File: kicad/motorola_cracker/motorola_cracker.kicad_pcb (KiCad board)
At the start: 2 copper layers, 134 x 39.4 mm, 27 parts, among them J1 DB9, P1 CONN_6, P2 CONN_2, P3 CONN_6, U1 78L10, U2 74LS245, U3 MAX232, U4 78L05, U5 68HC05_PLCC, X1 4Mhz

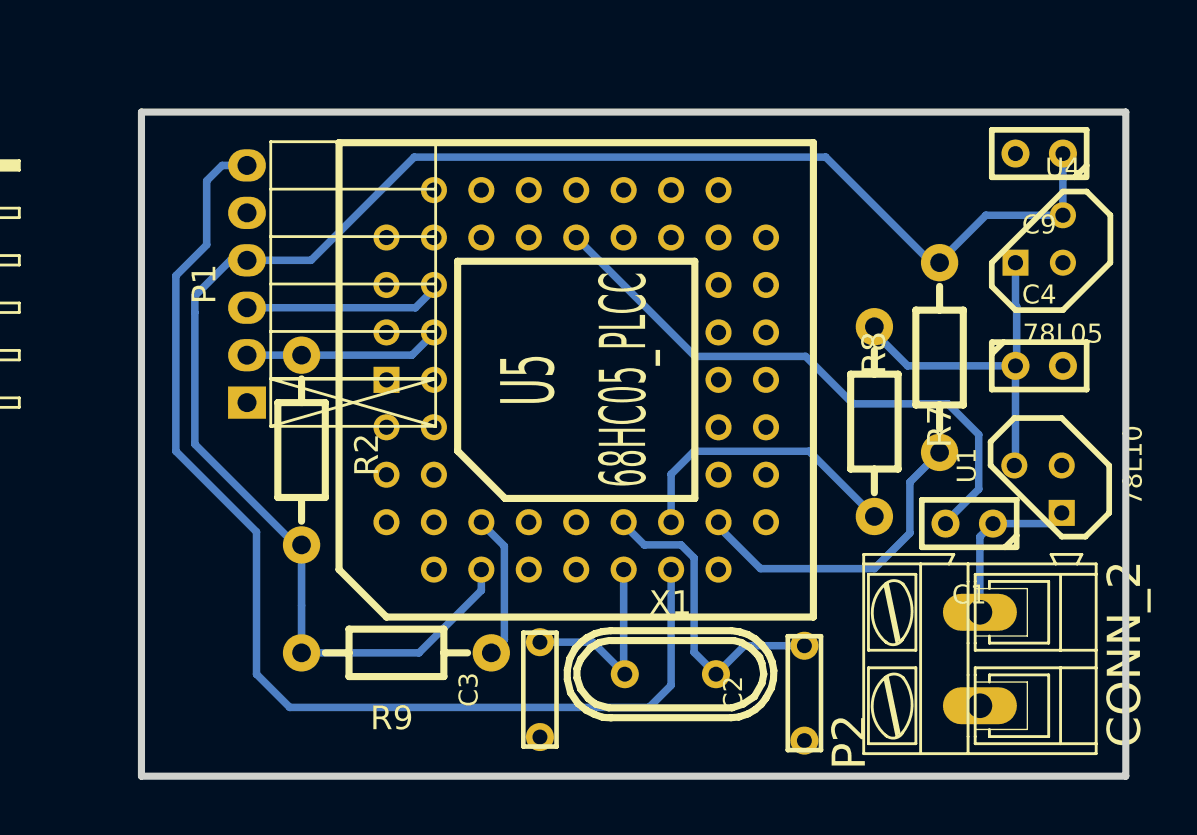
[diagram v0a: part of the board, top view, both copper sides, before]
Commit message: update cpu board to fit 50x50cm for dirtypcb servis req.
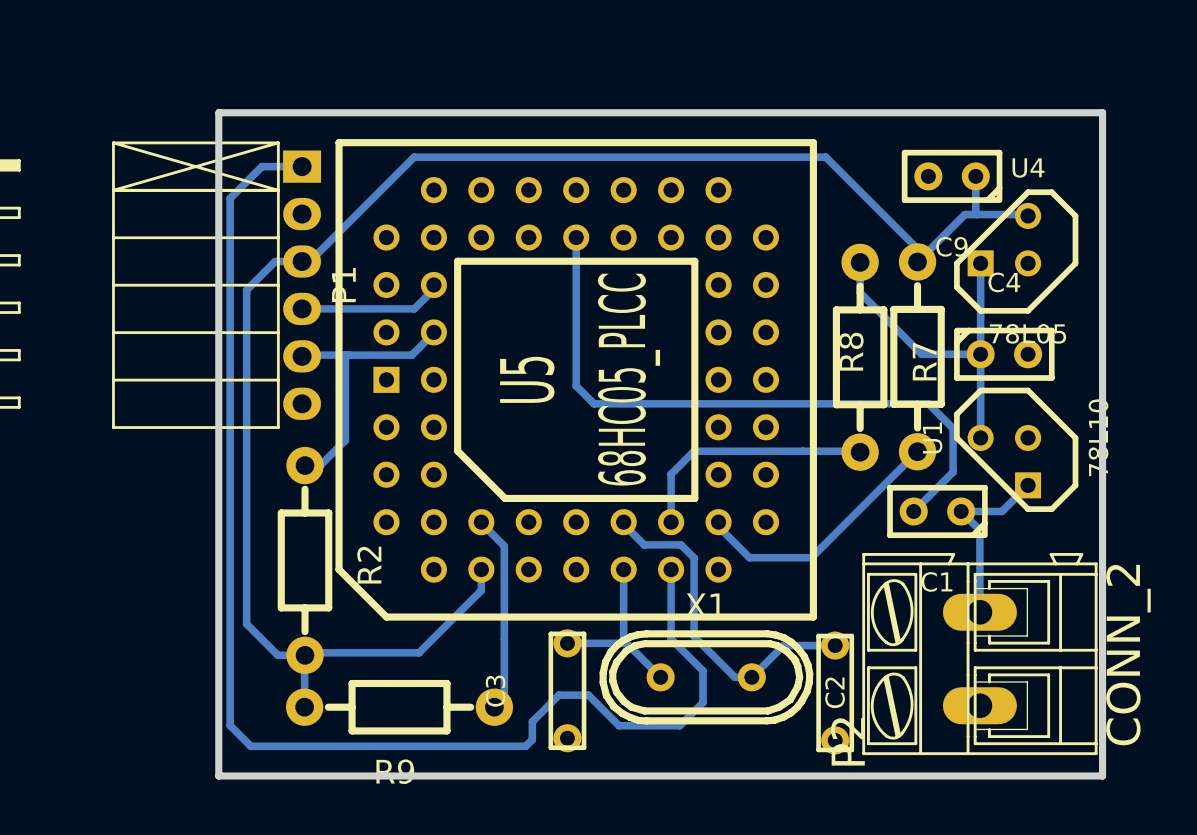
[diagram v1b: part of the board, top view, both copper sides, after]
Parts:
- moved R2 5.91 mm to (189.1, 108.5)
- moved C9 4.82 mm to (223.7, 87.9)
- moved R7 3.53 mm to (218.8, 97.6)
- moved P1 2.95 mm to (188.9, 93.7), turned to 90 degrees
- moved R9 2.92 mm to (194.2, 116.3)
- moved U1 2.33 mm to (226.5, 103.2)
- moved C4 1.97 mm to (226.5, 97.4)
- moved X1 1.93 mm to (210.6, 114.7)
- moved U4 1.87 mm to (226.5, 91.3)
- moved C1 1.82 mm to (223.0, 105.8)
- moved C2 1.65 mm to (217.5, 115.6)
- moved C3 1.47 mm to (203.1, 115.4)
- moved R8 1.18 mm to (221.9, 97.6)
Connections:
- net Tx renamed TX
- P1 pad 1: GND -> 68_18
- P1 pad 2: 68_52 -> (no net)
- P1 pad 3: 68_50 -> +5V
- P1 pad 4: +5V -> 68_50
- P1 pad 5: (no net) -> 68_52
- P1 pad 6: 68_18 -> GND
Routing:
- net 68_18: track 85.2 -> 93.5 mm
- net 68_52: track 22.0 -> 26.7 mm
- net Net-(R8-Pad1): track 17.4 -> 14.1 mm
- net GND: track 32.6 -> 35.8 mm
- net 68_50: track 22.1 -> 19.4 mm
- net +5V: track 114.9 -> 112.5 mm
- net Net-(R7-Pad2): track 15.5 -> 13.3 mm
- net Net-(R9-Pad1): track 9.29 -> 11.1 mm
- net Net-(C2-Pad2): track 17.1 -> 18.4 mm
- net Net-(C3-Pad2): track 10.9 -> 9.73 mm
- net Net-(C1-Pad1): track 8.96 -> 9.97 mm
- net +10V: track 19.5 -> 18.8 mm
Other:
- board size 134 x 39.4 mm -> 132.7 x 39.4 mm

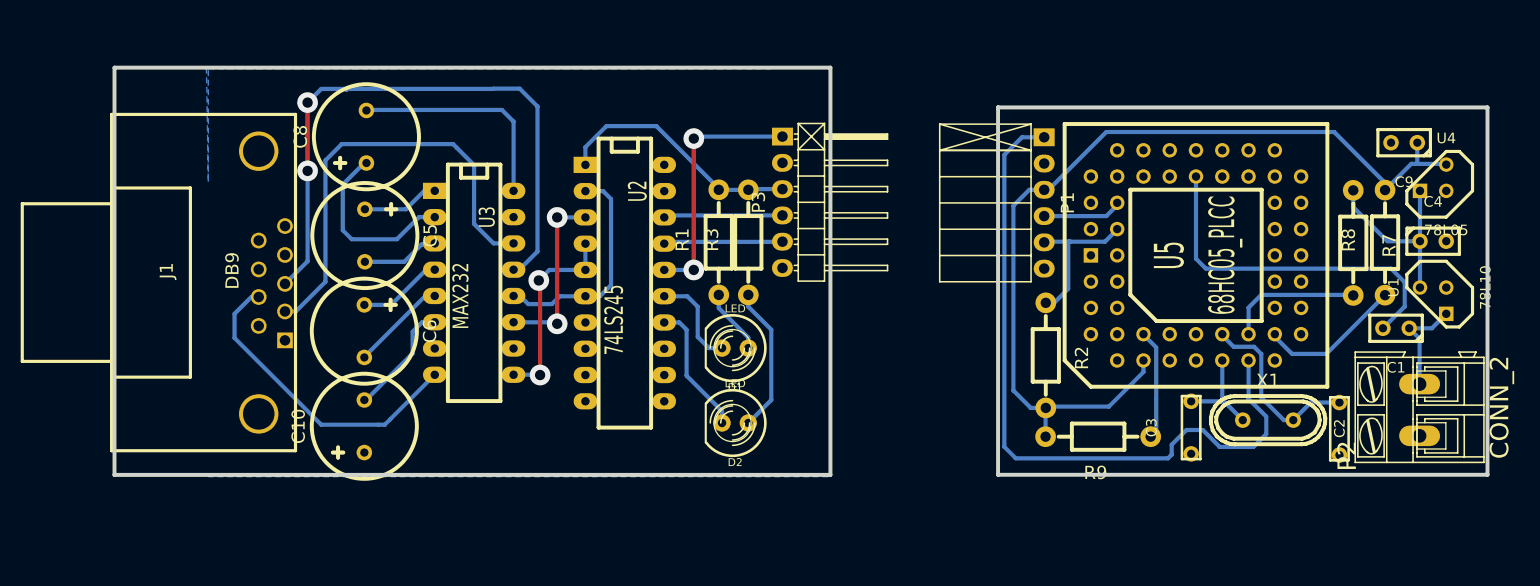
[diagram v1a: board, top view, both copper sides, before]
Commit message: remke pcb's to match 5x5cm
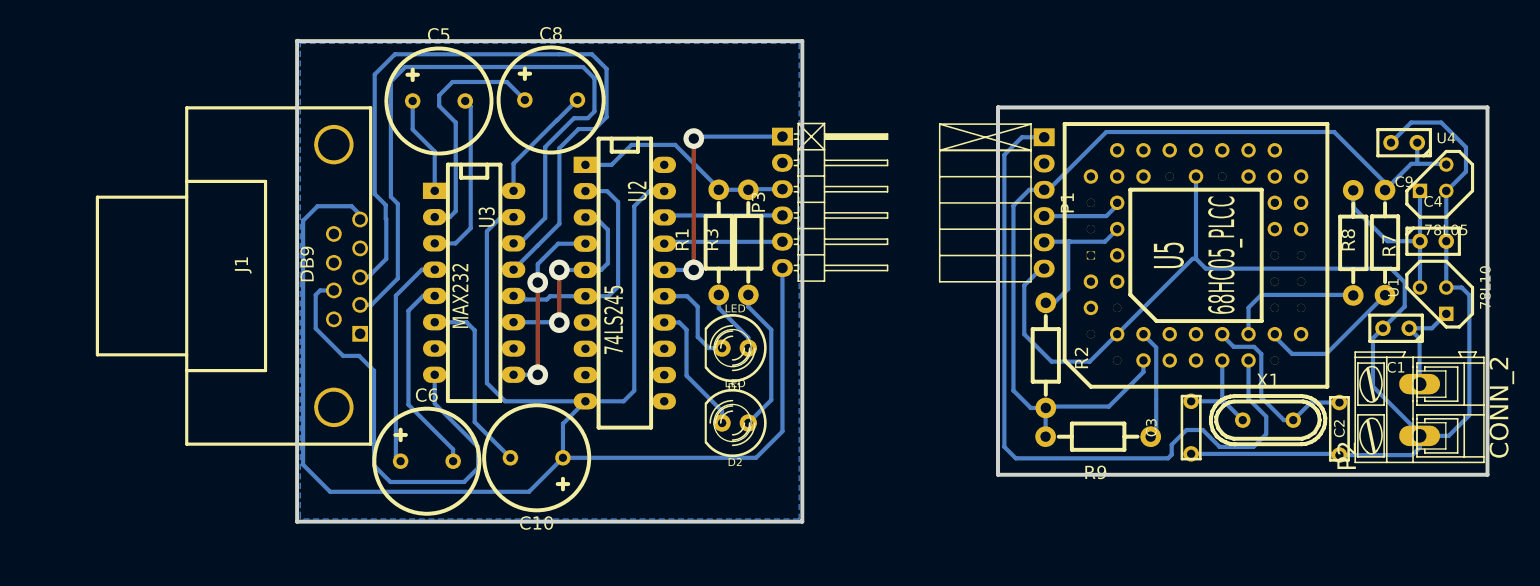
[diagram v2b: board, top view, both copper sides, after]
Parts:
- moved C8 18.2 mm to (141.3, 83.8), turned to 0 degrees
- moved C10 16.9 mm to (139.9, 118.4), turned to 180 degrees
- moved C5 14.8 mm to (130.4, 83.9), turned to 0 degrees
- moved C6 14.0 mm to (129.3, 118.7), turned to 0 degrees
- moved J1 7.29 mm to (121.5, 100.9)
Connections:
- U2 pad 5: Reset -> TX
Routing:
- net GND: track 35.8 -> 300.5 mm
- net Net-(J1-Pad2): track 43.0 -> 65.7 mm
- net Net-(C6-Pad1): track 8.22 -> 21.8 mm
- net Net-(J1-Pad7): track 30.2 -> 43.7 mm
- net Net-(C6-Pad2): track 9.30 -> 20.4 mm
- net Net-(J1-Pad3): track 59.4 -> 69.5 mm, vias 2 -> 0
- net Net-(C8-Pad2): track 21.4 -> 11.4 mm
- net Net-(C5-Pad2): track 7.49 -> 16.7 mm
- net Net-(C10-Pad2): track 11.3 -> 18.1 mm
- net Net-(C8-Pad1): track 17.7 -> 23.7 mm
- net TX: track 17.4 -> 20.5 mm
- net +5V: track 112.5 -> 110.0 mm
- net Net-(C5-Pad1): track 7.49 -> 9.57 mm
- net Reset: track 20.2 -> 18.5 mm
- net Rx: track 21.9 -> 22.8 mm
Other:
- board size 132.7 x 39.4 mm -> 115.1 x 46.5 mm
- net class Default: via_dia 2 -> 2.4; via_drill 1 -> 1.2

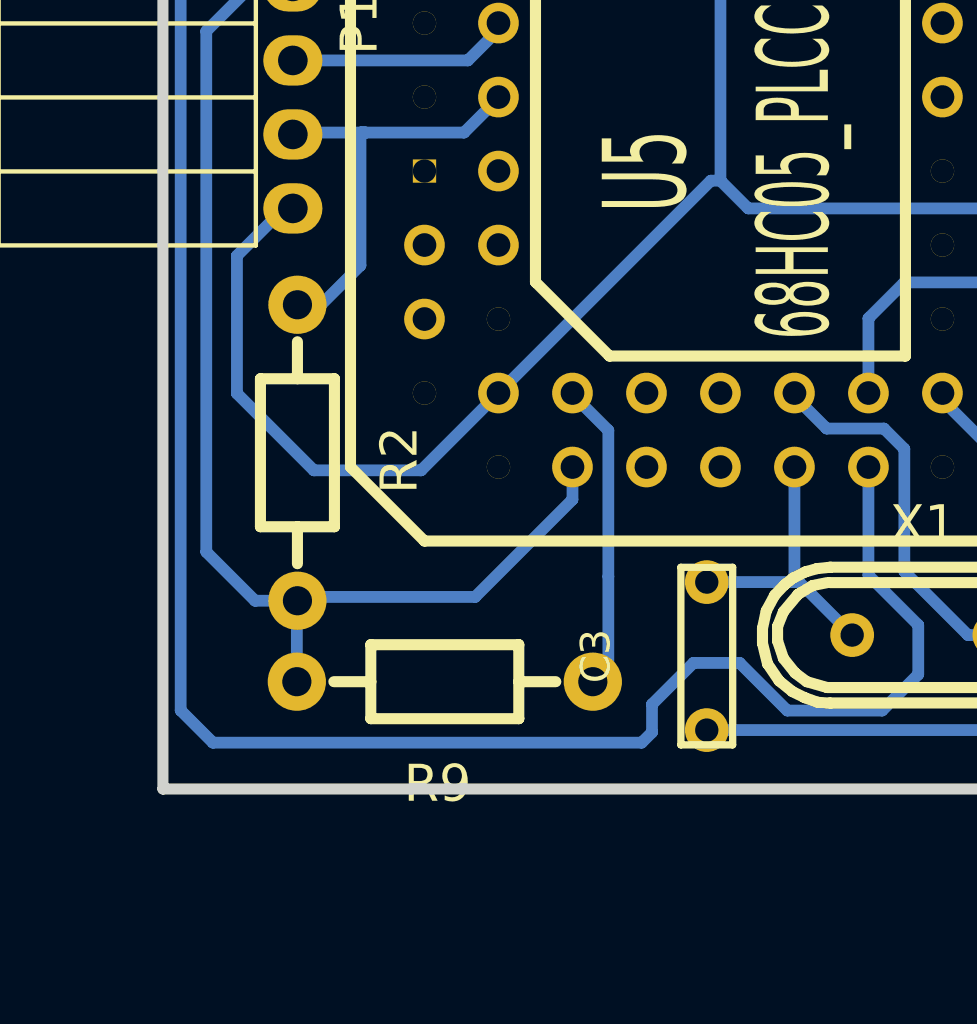
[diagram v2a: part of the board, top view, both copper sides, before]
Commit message: added switch to select 68HC05/68HC705 based on schematics mc68hc05-705.JPG
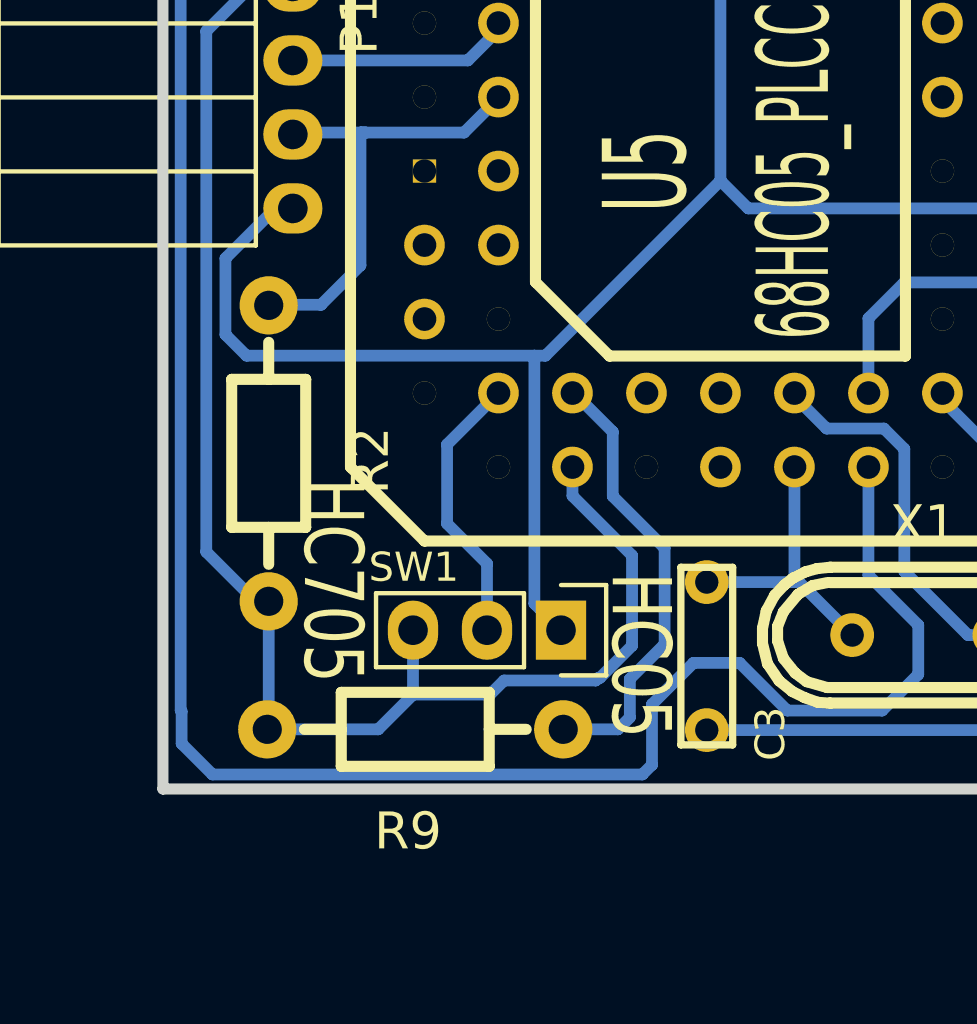
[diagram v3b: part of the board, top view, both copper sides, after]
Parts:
- added SW1: SWITCH_INV, Pin_Headers:Pin_Header_Straight_1x03, F.Cu at (198.1, 114.6)
- moved R9 1.93 mm to (193.1, 118.0)
- moved R2 0.99 mm to (188.1, 108.5)
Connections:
- net TX renamed Tx
- U5 pad 9: GND -> Net-(SW1-Pad2)
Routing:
- net +5V: track 110.0 -> 120.8 mm
- net Net-(SW1-Pad2): track 0.00 -> 9.44 mm
- net GND: track 300.5 -> 306.8 mm
- net Net-(R9-Pad1): track 11.1 -> 16.0 mm
- net 68_18: track 93.5 -> 95.7 mm
- net 68_52: track 26.7 -> 27.7 mm
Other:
- board text added: "HC05"
- board text added: "HC705"

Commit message: motorola cracker simple board for usb to serial dongle (tested with cp2102)
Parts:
- removed C10, C6, C8: 10m, Capacitors_Elko_ThroughHole:Elko_vert_DM10_RM5
- removed D1, D2: LED, LEDs:LED-5MM
- removed J1: DB9, Connect:DB9FC
- removed R3: 1k, Resistors_ThroughHole:Resistor_Horizontal_RM10mm
- removed SW1: SWITCH_INV, Pin_Headers:Pin_Header_Straight_1x03
- removed U3: MAX232, Sockets_DIP:DIP-16__300_ELL
- removed U5: 68HC05_PLCC, Sockets:PLCC52
- added JP1: JUMPER3, Pin_Headers:Pin_Header_Straight_1x03, F.Cu at (186.4, 117.9)
- C1, C4: footprint Capacitors_ThroughHole:Capacitor3MMDiscRM2.5 -> Capacitors_ThroughHole:C_Disc_D3_P2.5
- C2, C3: footprint Capacitors_ThroughHole:Capacitor6MMDiscRM5 -> Capacitors_ThroughHole:C_Rect_L7_W2_P5
- C5: value 10m -> 100n; footprint Capacitors_Elko_ThroughHole:Elko_vert_DM10_RM5 -> Capacitors_ThroughHole:C_Disc_D3_P2.5
- P1: value CONN_6 -> CONN_4; footprint Socket_Strips:Socket_Strip_Angled_1x06 -> Pin_Headers:Pin_Header_Straight_1x04
- P2: value CONN_2 -> CONN_1
- P3: value CONN_6 -> CONN_5; footprint Pin_Headers:Pin_Header_Angled_1x06 -> Pin_Headers:Pin_Header_Straight_1x01
- R1: value 1k -> 10k
- R2: value 4k7 -> 100M
- R8, R9: value 2k -> 1k
- U2: value 74LS245 -> 68HC05_PLCC; footprint Sockets_DIP:DIP-20__300_ELL -> Sockets:PLCC52
- moved C5 71.0 mm to (195.2, 112.9), turned to 180 degrees
- moved U2 55.3 mm to (203.6, 98.8), turned to 90 degrees
- moved P3 40.3 mm to (196.4, 117.1), turned to 0 degrees
- moved R1 29.5 mm to (186.2, 104.5)
- moved R2 22.4 mm to (210.1, 112.9), turned to 180 degrees
- moved C2 15.3 mm to (202.4, 117.9)
- moved C3 14.8 mm to (217.7, 117.9)
- moved R9 14.0 mm to (189.2, 104.6), turned to 90 degrees
- moved P1 7.21 mm to (186.6, 86.9), turned to 0 degrees
- moved R7 3.30 mm to (222.1, 97.7)
- moved R8 3.16 mm to (218.7, 97.7), turned to 270 degrees
- moved X1 2.24 mm to (210.1, 116.9), turned to 180 degrees
- moved C1 1.35 mm to (224.3, 105.8)
- turned C9 to 0 degrees
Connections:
- net +10V renamed /+10V
- C5 pad 1: Net-(C5-Pad1) -> +5V
- C5 pad 2: Net-(C5-Pad2) -> GND
- P1 pad 1: 68_18 -> /TX
- P1 pad 2: (no net) -> /RX
- P1 pad 4: 68_50 -> GND
- P3 pad 1: 68_18 -> /RESET
- R1 pad 1: Net-(D1-Pad1) -> Net-(JP1-Pad1)
- R2 pad 1: 68_52 -> Net-(C3-Pad2)
- R2 pad 2: +5V -> Net-(C2-Pad2)
- R8 pad 1: Net-(R8-Pad1) -> +5V
- R8 pad 2: +5V -> Net-(R8-Pad2)
- U2 pad 10: GND -> +5V
- U2 pad 11: (no net) -> Net-(R9-Pad1)
- U2 pad 14: Net-(D2-Pad2) -> (no net)
- U2 pad 15: Net-(D1-Pad2) -> (no net)
- U2 pad 16: 68_18 -> Net-(C2-Pad2)
- U2 pad 17: 68_52 -> Net-(C3-Pad2)
- U2 pad 18: 68_50 -> /RESET
- U2 pad 19: GND -> Net-(R7-Pad2)
- U2 pad 2: Rx -> (no net)
- U2 pad 3: Tx -> (no net)
- U2 pad 4: Reset -> (no net)
- U2 pad 5: Tx -> (no net)
- U2 pad 6: Rx -> (no net)
- U2 pad 9: (no net) -> Net-(JP1-Pad1)
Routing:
- net GND: track 306.8 -> 29.5 mm
- net 68_18: track 95.7 -> 0.00 mm, vias 2 -> 0
- net Net-(J1-Pad3): track 69.5 -> 0.00 mm
- net Net-(J1-Pad2): track 65.7 -> 0.00 mm
- net Net-(J1-Pad7): track 43.7 -> 0.00 mm
- net +5V: track 120.8 -> 78.1 mm
- net 68_52: track 27.7 -> 0.00 mm
- net /RESET: track 0.00 -> 24.5 mm
- net Net-(C8-Pad1): track 23.7 -> 0.00 mm
- net Rx: track 22.8 -> 0.00 mm
- net Net-(JP1-Pad1): track 0.00 -> 22.4 mm
- net Net-(C6-Pad1): track 21.8 -> 0.00 mm
- net Tx: track 20.5 -> 0.00 mm, vias 2 -> 0
- net Net-(C6-Pad2): track 20.4 -> 0.00 mm
- net /TX: track 0.00 -> 19.9 mm
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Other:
- board size 115.1 x 46.5 mm -> 47.3 x 35.5 mm

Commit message: simplified version
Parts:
- removed C1, C4, C5: 100n, Capacitors_ThroughHole:C_Disc_D3_P2.5
- removed C9: 100n, Capacitors_ThroughHole:Capacitor3MMDiscRM2.5
- removed U1: 78L10, my_modules:TO92-STABIL
- removed U4: 78L05, my_modules:TO92-STABIL
- C2, C3: footprint Capacitors_ThroughHole:C_Rect_L7_W2_P5 -> Capacitors_SMD:C_1206; moved to B.Cu
- P1: value CONN_4 -> UART
- P2: value CONN_1 -> +12V; footprint Connect:AK300-2 -> Socket_Strips:Socket_Strip_Straight_1x02
- P3: value CONN_5 -> RTS
- R1, R2, R7, R8, R9: footprint Resistors_ThroughHole:Resistor_Horizontal_RM10mm -> Resistors_SMD:R_1206; moved to B.Cu
- moved C3 20.0 mm to (206.2, 101.6), turned to 270 degrees
- moved R7 14.9 mm to (214.2, 110.3), turned to 180 degrees
- moved P3 12.7 mm to (208.7, 113.5)
- moved R8 12.7 mm to (206.1, 97.2), turned to 0 degrees
- moved X1 12.6 mm to (198.1, 113.1), turned to 0 degrees
- moved P2 12.6 mm to (212.6, 113.4), turned to 0 degrees
- moved R9 12.3 mm to (200.0, 98.8)
- moved JP1 9.16 mm to (189.1, 109.1), turned to 0 degrees
- moved R2 8.88 mm to (201.5, 110.6), turned to 0 degrees
- moved P1 8.57 mm to (189.1, 95.1), turned to 180 degrees
- moved C2 5.87 mm to (205.1, 112.6)
- moved R1 3.70 mm to (189.8, 103.9)
- moved U2 1.08 mm to (203.6, 97.7)
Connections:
- P2 pad 2: Net-(C1-Pad1) -> /+12V
- R7 pad 1: /+10V -> /+12V
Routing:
- net GND: track 29.5 -> 90.7 mm
- net +5V: track 78.1 -> 52.5 mm
- net /RESET: track 24.5 -> 5.91 mm
- net Net-(R7-Pad2): track 21.7 -> 7.96 mm
- net /+10V: track 12.5 -> 0.00 mm
- net /TX: track 19.9 -> 7.86 mm
- net Net-(C1-Pad1): track 9.97 -> 0.00 mm
- net Net-(JP1-Pad1): track 22.4 -> 12.5 mm
- net Net-(R9-Pad1): track 11.0 -> 5.76 mm
- net Net-(C3-Pad2): track 21.5 -> 17.4 mm
- net /+12V: track 0.00 -> 3.70 mm
- net /RX: track 11.6 -> 8.22 mm
- net Net-(R8-Pad2): track 12.7 -> 10.3 mm
- net Net-(C2-Pad2): track 12.1 -> 10.6 mm
- removed copper zone on B.Cu, net GND
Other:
- board size 47.3 x 35.5 mm -> 29.5 x 31.6 mm
- board text removed: "HC05"
- board text removed: "HC705"
